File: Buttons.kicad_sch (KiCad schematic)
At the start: 24 parts, among them SW1 SW_PUSHBUTTON, SW2 SW_PUSHBUTTON, SW3 SW_PUSHBUTTON, SW4 SW_PUSHBUTTON, SW5 SW_PUSHBUTTON, SW6 SW_PUSHBUTTON

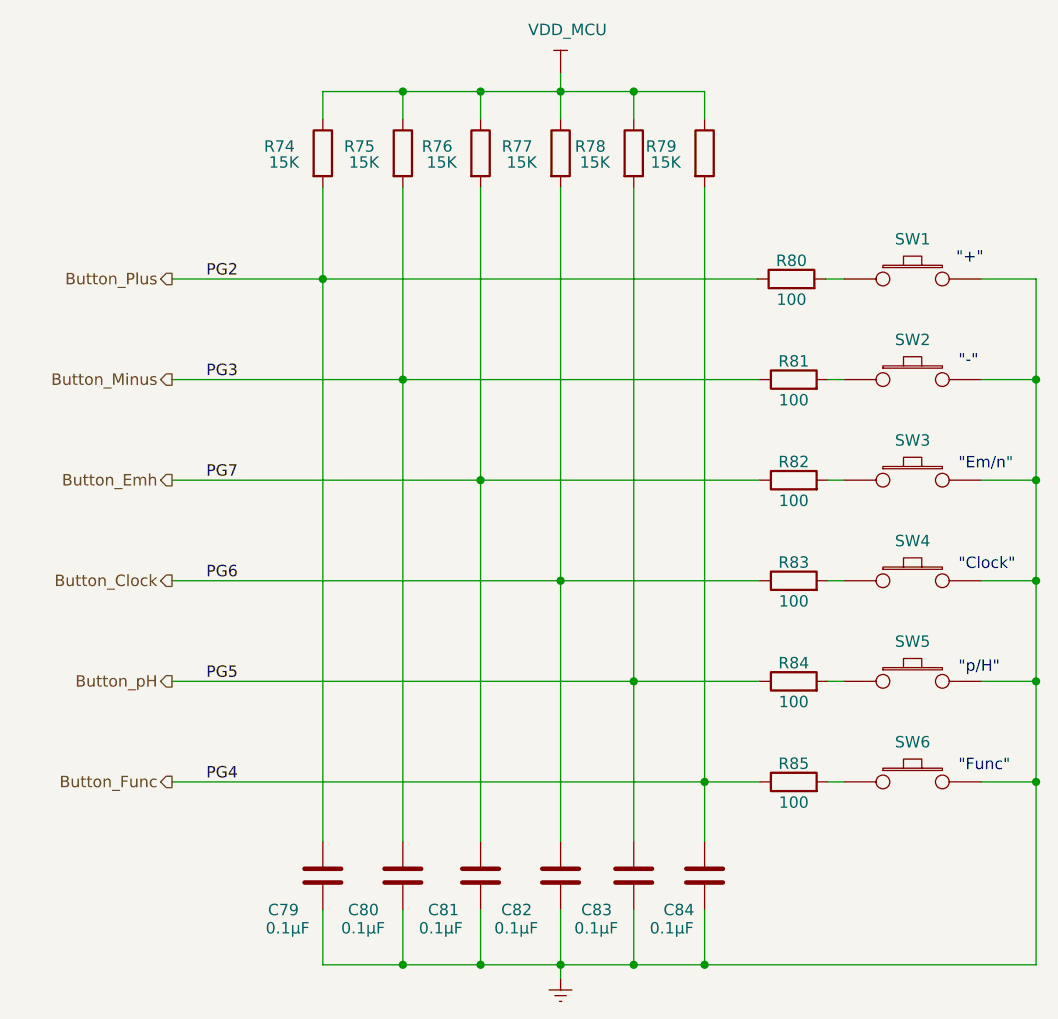
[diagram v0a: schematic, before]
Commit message: KiCAD6.0 scheema rules check done
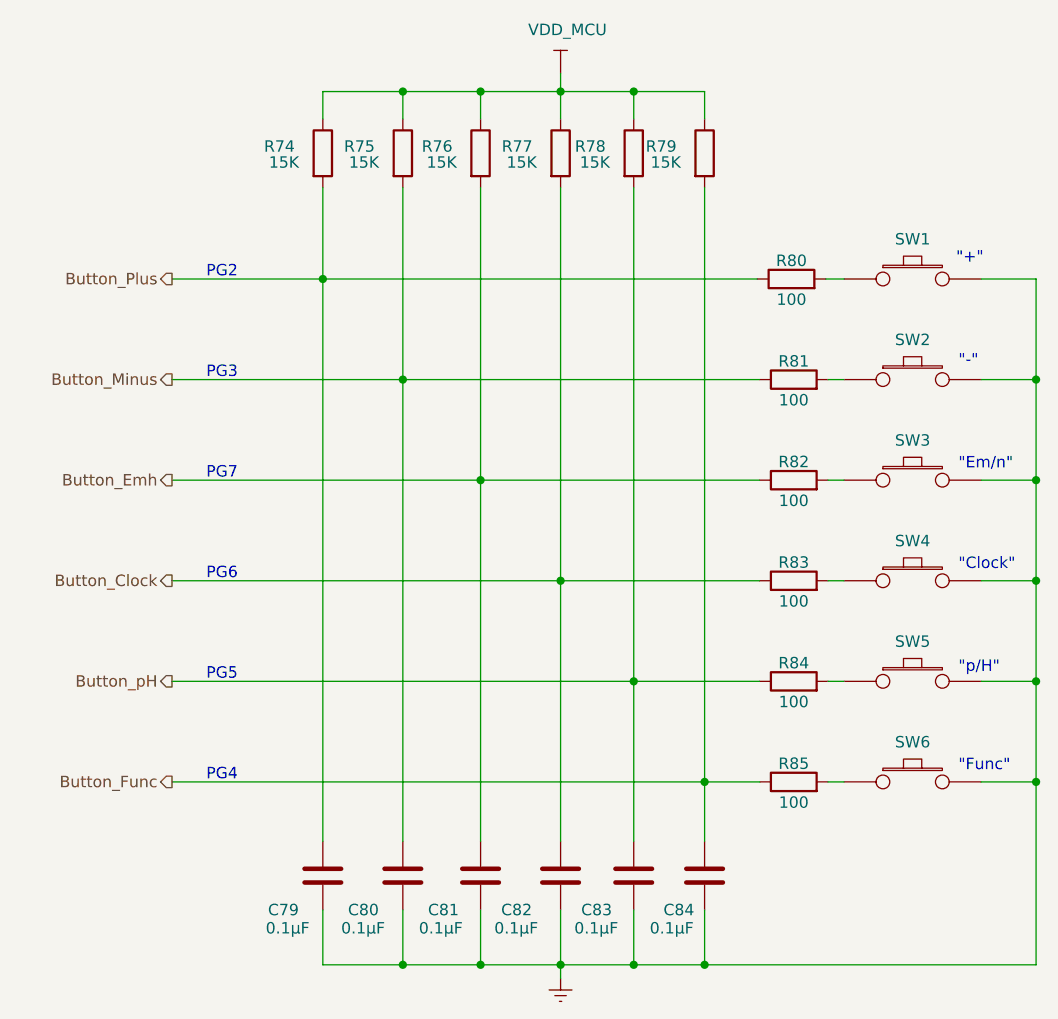
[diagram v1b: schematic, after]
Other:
- note added: "PG2"
- note added: "PG3"
- note added: "PG4"
- note added: "PG5"
- note added: "PG6"
- note added: "PG7"
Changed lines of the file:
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@@
+    (effects (font (size 1.27 1.27)) (justify left bottom))
+  )
+  (text "PG4" (at 97.028 107.442 0)
     (effects (font (size 1.27 1.27)) (justify left bottom))
   )
   (text "\"Em/n\"" (at 180.594 72.898 0)
+    (effects (font (size 1.27 1.27)) (justify left bottom))
+  )
+  (text "PG7" (at 97.028 73.914 0)
     (effects (font (size 1.27 1.27)) (justify left bottom))
   )
@@
     (effects (font (size 1.27 1.27)) (justify left bottom))
   )
+  (text "PG6" (at 97.028 85.09 0)
+    (effects (font (size 1.27 1.27)) (justify left bottom))
+  )
+  (text "PG3" (at 97.028 62.738 0)
+    (effects (font (size 1.27 1.27)) (justify left bottom))
+  )
   (text "\"Clock\"" (at 180.594 84.074 0)
+    (effects (font (size 1.27 1.27)) (justify left bottom))
+  )
+  (text "PG5\n" (at 97.028 96.266 0)
     (effects (font (size 1.27 1.27)) (justify left bottom))
   )
@@
     (effects (font (size 1.27 1.27)) (justify left bottom))
   )
-  (label "PG3" (at 97.028 62.738 0)
+  (text "PG2" (at 97.028 51.562 0)
     (effects (font (size 1.27 1.27)) (justify left bottom))
   )
-  (label "PG5" (at 97.028 96.266 0)
-    (effects (font (size 1.27 1.27)) (justify left bottom))
-  )
-  (label "PG4" (at 97.028 107.442 0)
-    (effects (font (size 1.27 1.27)) (justify left bottom))
-  )
-  (label "PG7" (at 97.028 73.914 0)
-    (effects (font (size 1.27 1.27)) (justify left bottom))
-  )
-  (label "PG6" (at 97.028 85.09 0)
-    (effects (font (size 1.27 1.27)) (justify left bottom))
-  )
-  (label "PG2" (at 97.028 51.562 0)
-    (effects (font (size 1.27 1.27)) (justify left bottom))
-  )

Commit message: All handsolder footprints removed
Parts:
- C79, C80, C81, C82, C83, C84: footprint Capacitor_SMD:C_0603_1608Metric_Pad1.08x0.95mm_HandSolder -> Capacitor_SMD:C_0603_1608Metric
- R74, R75, R76, R77, R78, R79, R80, R81, R82, R83, R84, R85: footprint Resistor_SMD:R_0805_2012Metric_Pad1.20x1.40mm_HandSolder -> Resistor_SMD:R_0805_2012Metric
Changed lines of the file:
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@@
     (property "Reference" "R79" (id 0) (at 147.574 36.83 0))
     (property "Value" "15K" (id 1) (at 148.082 38.608 0))
-    (property "Footprint" "Resistor_SMD:R_0805_2012Metric_Pad1.20x1.40mm_HandSolder" (id 2) (at 150.622 37.592 90)
+    (property "Footprint" "Resistor_SMD:R_0805_2012Metric" (id 2) (at 150.622 37.592 90)
       (effects (font (size 1.27 1.27)) hide)
     )
@@
     (property "Reference" "R78" (id 0) (at 139.7 36.83 0))
     (property "Value" "15K" (id 1) (at 140.208 38.608 0))
-    (property "Footprint" "Resistor_SMD:R_0805_2012Metric_Pad1.20x1.40mm_HandSolder" (id 2) (at 142.748 37.592 90)
+    (property "Footprint" "Resistor_SMD:R_0805_2012Metric" (id 2) (at 142.748 37.592 90)
       (effects (font (size 1.27 1.27)) hide)
     )
@@
     (property "Reference" "R77" (id 0) (at 131.572 36.83 0))
     (property "Value" "15K" (id 1) (at 132.08 38.608 0))
-    (property "Footprint" "Resistor_SMD:R_0805_2012Metric_Pad1.20x1.40mm_HandSolder" (id 2) (at 134.62 37.592 90)
+    (property "Footprint" "Resistor_SMD:R_0805_2012Metric" (id 2) (at 134.62 37.592 90)
       (effects (font (size 1.27 1.27)) hide)
     )
@@
     (property "Reference" "R76" (id 0) (at 122.682 36.83 0))
     (property "Value" "15K" (id 1) (at 123.19 38.608 0))
-    (property "Footprint" "Resistor_SMD:R_0805_2012Metric_Pad1.20x1.40mm_HandSolder" (id 2) (at 125.73 37.592 90)
+    (property "Footprint" "Resistor_SMD:R_0805_2012Metric" (id 2) (at 125.73 37.592 90)
       (effects (font (size 1.27 1.27)) hide)
     )
@@
     (property "Reference" "R75" (id 0) (at 114.046 36.83 0))
     (property "Value" "15K" (id 1) (at 114.554 38.608 0))
-    (property "Footprint" "Resistor_SMD:R_0805_2012Metric_Pad1.20x1.40mm_HandSolder" (id 2) (at 117.094 37.592 90)
+    (property "Footprint" "Resistor_SMD:R_0805_2012Metric" (id 2) (at 117.094 37.592 90)
       (effects (font (size 1.27 1.27)) hide)
     )
@@
     (property "Reference" "R74" (id 0) (at 105.156 36.83 0))
     (property "Value" "15K" (id 1) (at 105.664 38.608 0))
-    (property "Footprint" "Resistor_SMD:R_0805_2012Metric_Pad1.20x1.40mm_HandSolder" (id 2) (at 108.204 37.592 90)
+    (property "Footprint" "Resistor_SMD:R_0805_2012Metric" (id 2) (at 108.204 37.592 90)
       (effects (font (size 1.27 1.27)) hide)
     )
@@
     (property "Reference" "R80" (id 0) (at 162.052 49.53 90))
     (property "Value" "100" (id 1) (at 162.052 53.848 90))
-    (property "Footprint" "Resistor_SMD:R_0805_2012Metric_Pad1.20x1.40mm_HandSolder" (id 2) (at 162.052 53.34 90)
+    (property "Footprint" "Resistor_SMD:R_0805_2012Metric" (id 2) (at 162.052 53.34 90)
       (effects (font (size 1.27 1.27)) hide)
     )
@@
       (effects (font (size 1.27 1.27)) (justify left))
     )
-    (property "Footprint" "Capacitor_SMD:C_0603_1608Metric_Pad1.08x0.95mm_HandSolder" (id 2) (at 110.9472 121.666 0)
+    (property "Footprint" "Capacitor_SMD:C_0603_1608Metric" (id 2) (at 110.9472 121.666 0)
       (effects (font (size 1.27 1.27)) hide)
     )
@@
       (effects (font (size 1.27 1.27)) (justify left))
     )
-    (property "Footprint" "Capacitor_SMD:C_0603_1608Metric_Pad1.08x0.95mm_HandSolder" (id 2) (at 119.8372 121.666 0)
+    (property "Footprint" "Capacitor_SMD:C_0603_1608Metric" (id 2) (at 119.8372 121.666 0)
       (effects (font (size 1.27 1.27)) hide)
     )
@@
       (effects (font (size 1.27 1.27)) (justify left))
     )
-    (property "Footprint" "Capacitor_SMD:C_0603_1608Metric_Pad1.08x0.95mm_HandSolder" (id 2) (at 128.4732 121.666 0)
+    (property "Footprint" "Capacitor_SMD:C_0603_1608Metric" (id 2) (at 128.4732 121.666 0)
       (effects (font (size 1.27 1.27)) hide)
     )
@@
       (effects (font (size 1.27 1.27)) (justify left))
     )
-    (property "Footprint" "Capacitor_SMD:C_0603_1608Metric_Pad1.08x0.95mm_HandSolder" (id 2) (at 137.3632 121.666 0)
+    (property "Footprint" "Capacitor_SMD:C_0603_1608Metric" (id 2) (at 137.3632 121.666 0)
       (effects (font (size 1.27 1.27)) hide)
     )
@@
       (effects (font (size 1.27 1.27)) (justify left))
     )
-    (property "Footprint" "Capacitor_SMD:C_0603_1608Metric_Pad1.08x0.95mm_HandSolder" (id 2) (at 145.4912 121.666 0)
+    (property "Footprint" "Capacitor_SMD:C_0603_1608Metric" (id 2) (at 145.4912 121.666 0)
       (effects (font (size 1.27 1.27)) hide)
     )
@@
       (effects (font (size 1.27 1.27)) (justify left))
     )
-    (property "Footprint" "Capacitor_SMD:C_0603_1608Metric_Pad1.08x0.95mm_HandSolder" (id 2) (at 153.3652 121.666 0)
+    (property "Footprint" "Capacitor_SMD:C_0603_1608Metric" (id 2) (at 153.3652 121.666 0)
       (effects (font (size 1.27 1.27)) hide)
     )
@@
     (property "Reference" "R81" (id 0) (at 162.306 60.706 90))
     (property "Value" "100" (id 1) (at 162.306 65.024 90))
-    (property "Footprint" "Resistor_SMD:R_0805_2012Metric_Pad1.20x1.40mm_HandSolder" (id 2) (at 162.306 64.516 90)
+    (property "Footprint" "Resistor_SMD:R_0805_2012Metric" (id 2) (at 162.306 64.516 90)
       (effects (font (size 1.27 1.27)) hide)
     )
@@
     (property "Reference" "R82" (id 0) (at 162.306 71.882 90))
     (property "Value" "100" (id 1) (at 162.306 76.2 90))
-    (property "Footprint" "Resistor_SMD:R_0805_2012Metric_Pad1.20x1.40mm_HandSolder" (id 2) (at 162.306 75.692 90)
+    (property "Footprint" "Resistor_SMD:R_0805_2012Metric" (id 2) (at 162.306 75.692 90)
       (effects (font (size 1.27 1.27)) hide)
     )
@@
     (property "Reference" "R83" (id 0) (at 162.306 83.058 90))
     (property "Value" "100" (id 1) (at 162.306 87.376 90))
-    (property "Footprint" "Resistor_SMD:R_0805_2012Metric_Pad1.20x1.40mm_HandSolder" (id 2) (at 162.306 86.868 90)
+    (property "Footprint" "Resistor_SMD:R_0805_2012Metric" (id 2) (at 162.306 86.868 90)
       (effects (font (size 1.27 1.27)) hide)
     )
@@
     (property "Reference" "R84" (id 0) (at 162.306 94.234 90))
     (property "Value" "100" (id 1) (at 162.306 98.552 90))
-    (property "Footprint" "Resistor_SMD:R_0805_2012Metric_Pad1.20x1.40mm_HandSolder" (id 2) (at 162.306 98.044 90)
+    (property "Footprint" "Resistor_SMD:R_0805_2012Metric" (id 2) (at 162.306 98.044 90)
       (effects (font (size 1.27 1.27)) hide)
     )
@@
     (property "Reference" "R85" (id 0) (at 162.306 105.41 90))
     (property "Value" "100" (id 1) (at 162.306 109.728 90))
-    (property "Footprint" "Resistor_SMD:R_0805_2012Metric_Pad1.20x1.40mm_HandSolder" (id 2) (at 162.306 109.22 90)
-      (effects (font (size 1.27 1.27)) hide)
-    )
+    (property "Footprint" "Resistor_SMD:R_0805_2012Metric" (id 2) (at 162.306 109.22 90)
+      (effects (font (size 1.27 1.27)) hide)
+    )
